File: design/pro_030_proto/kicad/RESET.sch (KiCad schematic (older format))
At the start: 13 parts, among them IC13 555N, IC8 74LS01N

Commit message: Add IO and XVID glue etc.
* Add IO Select glue
* Add Xosera glue
* Add new glues to schematic
* Clean up libs
* Reannotate (again)
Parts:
- renumbered C18 to C20, C19 to C21, IC8 to IC14, IC13 to IC15
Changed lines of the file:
@@
 AR Path="/5E53B952/6104F00C" Ref="IC?"  Part="1"
 AR Path="/60FBFA5C/6104F00C" Ref="IC?"  Part="1"
-AR Path="/61043B8D/6104F00C" Ref="IC13"  Part="1"
-F 0 "IC13" H 3850 4130 59  0000 L BNN
+AR Path="/61043B8D/6104F00C" Ref="IC15"  Part="1"
+F 0 "IC15" H 3850 4130 59  0000 L BNN
 F 1 "555N" H 3850 3195 59  0000 L BNN
 F 2 "Package_DIP:DIP-8_W7.62mm_LongPads" H 4150 3700 50  0001 C CNN
@@
 AR Path="/5E53B952/6104F012" Ref="IC?"  Part="1"
 AR Path="/60FBFA5C/6104F012" Ref="IC?"  Part="1"
-AR Path="/61043B8D/6104F012" Ref="IC8"  Part="1"
-F 0 "IC8" H 5900 4925 59  0000 L BNN
+AR Path="/61043B8D/6104F012" Ref="IC14"  Part="1"
+F 0 "IC14" H 5900 4925 59  0000 L BNN
 F 1 "74LS01N" H 5900 4600 59  0001 L BNN
 F 2 "Package_DIP:DIP-14_W7.62mm_Socket_LongPads" H 5800 4800 50  0001 C CNN
@@
 AR Path="/5E53B952/6104F018" Ref="IC?"  Part="2"
 AR Path="/60FBFA5C/6104F018" Ref="IC?"  Part="2"
-AR Path="/61043B8D/6104F018" Ref="IC8"  Part="2"
-F 0 "IC8" H 5900 5425 59  0000 L BNN
+AR Path="/61043B8D/6104F018" Ref="IC14"  Part="2"
+F 0 "IC14" H 5900 5425 59  0000 L BNN
 F 1 "74LS01N" H 5900 5100 59  0001 L BNN
 F 2 "Package_DIP:DIP-14_W7.62mm_Socket_LongPads" H 5800 5300 50  0001 C CNN
@@
 AR Path="/5E53B952/6104F01E" Ref="IC?"  Part="3"
 AR Path="/60FBFA5C/6104F01E" Ref="IC?"  Part="3"
-AR Path="/61043B8D/6104F01E" Ref="IC8"  Part="3"
-F 0 "IC8" H 6700 3825 59  0000 L BNN
+AR Path="/61043B8D/6104F01E" Ref="IC14"  Part="3"
+F 0 "IC14" H 6700 3825 59  0000 L BNN
 F 1 "74LS01N" H 6700 3500 59  0001 L BNN
 F 2 "Package_DIP:DIP-14_W7.62mm_Socket_LongPads" H 6600 3700 50  0001 C CNN
@@
 AR Path="/5E53B952/6104F048" Ref="C?"  Part="1"
 AR Path="/60FBFA5C/6104F048" Ref="C?"  Part="1"
-AR Path="/61043B8D/6104F048" Ref="C19"  Part="1"
-F 0 "C19" H 3210 2715 59  0000 L BNN
+AR Path="/61043B8D/6104F048" Ref="C21"  Part="1"
+F 0 "C21" H 3210 2715 59  0000 L BNN
 F 1 "100nF" H 3210 2515 59  0000 L BNN
 F 2 "Capacitor_THT:C_Rect_L4.0mm_W2.5mm_P2.50mm" H 3150 2700 50  0001 C CNN
@@
 AR Path="/5E53B952/6104F06C" Ref="C?"  Part="1"
 AR Path="/60FBFA5C/6104F06C" Ref="C?"  Part="1"
-AR Path="/61043B8D/6104F06C" Ref="C18"  Part="1"
-F 0 "C18" H 2795 4119 59  0000 L BNN
+AR Path="/61043B8D/6104F06C" Ref="C20"  Part="1"
+F 0 "C20" H 2795 4119 59  0000 L BNN
 F 1 "100uF" H 2795 3919 59  0000 L BNN
 F 2 "rosco_m68k:C-Electolytic-2,5-5" H 2750 4100 50  0001 C CNN
@@
 NoConn ~ 4550 3600
 $Comp
-L power:GND #PWR036
+L power:GND #PWR038
 U 1 1 6104F076
 P 4850 5700
-F 0 "#PWR036" H 4850 5450 50  0001 C CNN
+F 0 "#PWR038" H 4850 5450 50  0001 C CNN
 F 1 "GND" H 4855 5527 50  0000 C CNN
 F 2 "" H 4850 5700 50  0001 C CNN
@@
 	4850 5200 4850 5700
 $Comp
-L power:VCC #PWR034
+L power:VCC #PWR036
 U 1 1 6104F07D
 P 3550 2200
-F 0 "#PWR034" H 3550 2050 50  0001 C CNN
+F 0 "#PWR036" H 3550 2050 50  0001 C CNN
 F 1 "VCC" H 3567 2373 50  0000 C CNN
 F 2 "" H 3550 2200 50  0001 C CNN
@@
 $EndComp
 $Comp
-L power:VCC #PWR035
+L power:VCC #PWR037
 U 1 1 6104F083
 P 4650 2200
-F 0 "#PWR035" H 4650 2050 50  0001 C CNN
+F 0 "#PWR037" H 4650 2050 50  0001 C CNN
 F 1 "VCC" H 4667 2373 50  0000 C CNN
 F 2 "" H 4650 2200 50  0001 C CNN
@@
 $EndComp
 $Comp
-L power:VCC #PWR037
+L power:VCC #PWR039
 U 1 1 6104F089
 P 8500 2200
-F 0 "#PWR037" H 8500 2050 50  0001 C CNN
+F 0 "#PWR039" H 8500 2050 50  0001 C CNN
 F 1 "VCC" H 8517 2373 50  0000 C CNN
 F 2 "" H 8500 2200 50  0001 C CNN
@@
 	3550 2200 3550 3600
 $Comp
-L power:VCC #PWR033
+L power:VCC #PWR035
 U 1 1 6104F0A4
 P 3150 2200
-F 0 "#PWR033" H 3150 2050 50  0001 C CNN
+F 0 "#PWR035" H 3150 2050 50  0001 C CNN
 F 1 "VCC" H 3167 2373 50  0000 C CNN
 F 2 "" H 3150 2200 50  0001 C CNN
@@
 $EndComp
 $Comp
-L power:VCC #PWR032
+L power:VCC #PWR034
 U 1 1 6104F0AA
 P 2750 2200
-F 0 "#PWR032" H 2750 2050 50  0001 C CNN
+F 0 "#PWR034" H 2750 2050 50  0001 C CNN
 F 1 "VCC" H 2767 2373 50  0000 C CNN
 F 2 "" H 2750 2200 50  0001 C CNN

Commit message: Lots of work
* Sort out power and reset circuits, add ATX
* Add PCF8584 and supporting GAL code
* Stub out ATX board outline in PCB
* Various other tidying up and prep for layout
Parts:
- added unit 5 of IC14
- added J23: RESET_SW, Connector_PinHeader_2.54mm:PinHeader_2x01_P2.54mm_Vertical, symbol Connector:Conn_01x02_Male
- IC14: value 74LS01N -> 74LS05; symbol rosco_m68k-eagle-import:7401N -> 74xx:74LS05
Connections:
- net HALT: now also IC14.2, IC14.5; no longer IC14.1 (O), IC14.8 (I0), IC14.9 (I1)
- net at C20.+, IC15.2 (TR), IC15.6 (THR)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: now also IC14.10, J23.2 (Pin_2)
- net at LED1.K (C): now also IC14.6; no longer IC14.10 (O)
- net at R28.2, S1.3 (P): now also J23.1 (Pin_1)
- new net: IC14.1, IC14.3, IC15.3 (Q)
- new net PWR_GD: IC14.11
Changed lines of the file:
@@
 $Descr A4 11693 8268
 encoding utf-8
-Sheet 8 13
+Sheet 8 15
 Title "rosco_m68k Pro (030) Prototype"
-Date "2021-07-24"
+Date "2021-10-01"
 Rev "0"
 Comp "The Really Old-School Company Limited"
@@
 Wire Wire Line
 	6100 4800 6200 4800
-Wire Wire Line
-	6300 3800 6200 3800
-Wire Wire Line
-	6200 3800 6200 3600
-Wire Wire Line
-	6200 3600 6300 3600
-Connection ~ 6200 3800
 Text GLabel 9650 4800 2    67   Output ~ 0
 HALT
@@
 	7450 3200 7450 3000
 Wire Wire Line
-	5200 4800 5400 4800
-Wire Wire Line
-	5400 4800 5400 4700
-Wire Wire Line
-	5400 4700 5500 4700
-Wire Wire Line
-	5400 4800 5400 4900
-Wire Wire Line
-	5400 4900 5500 4900
-Wire Wire Line
 	5200 4800 5200 5300
-Wire Wire Line
-	5200 5300 5400 5300
-Wire Wire Line
-	5400 5300 5400 5200
-Wire Wire Line
-	5400 5200 5500 5200
-Wire Wire Line
-	5400 5300 5400 5400
-Wire Wire Line
-	5400 5400 5500 5400
-Connection ~ 5400 4800
-Connection ~ 5400 5300
 Connection ~ 5200 4800
 Wire Wire Line
-	4050 5200 4250 5200
+	4050 5200 4150 5200
 Wire Wire Line
 	4550 3800 4850 3800
@@
 	2350 4900 2350 3400
 Wire Wire Line
-	3650 5200 3050 5200
+	3650 5200 3350 5200
 Wire Wire Line
 	3050 5200 3050 4900
@@
 $EndComp
 $Comp
-L rosco_m68k-eagle-import:7401N IC?
+L 74xx:74LS05 IC?
 U 1 1 6104F012
 P 5800 4800
@@
 AR Path="/61043B8D/6104F012" Ref="IC14"  Part="1"
 F 0 "IC14" H 5900 4925 59  0000 L BNN
-F 1 "74LS01N" H 5900 4600 59  0001 L BNN
+F 1 "74LS05" H 5900 4600 59  0001 L BNN
 F 2 "Package_DIP:DIP-14_W7.62mm_Socket_LongPads" H 5800 4800 50  0001 C CNN
 F 3 "" H 5800 4800 50  0001 C CNN
@@
 $EndComp
 $Comp
-L rosco_m68k-eagle-import:7401N IC?
+L 74xx:74LS05 IC?
 U 2 1 6104F018
 P 5800 5300
@@
 AR Path="/61043B8D/6104F018" Ref="IC14"  Part="2"
 F 0 "IC14" H 5900 5425 59  0000 L BNN
-F 1 "74LS01N" H 5900 5100 59  0001 L BNN
+F 1 "74LS05" H 5900 5100 59  0001 L BNN
 F 2 "Package_DIP:DIP-14_W7.62mm_Socket_LongPads" H 5800 5300 50  0001 C CNN
 F 3 "" H 5800 5300 50  0001 C CNN
@@
 $EndComp
 $Comp
-L rosco_m68k-eagle-import:7401N IC?
+L 74xx:74LS05 IC?
 U 3 1 6104F01E
 P 6600 3700
@@
 AR Path="/61043B8D/6104F01E" Ref="IC14"  Part="3"
 F 0 "IC14" H 6700 3825 59  0000 L BNN
-F 1 "74LS01N" H 6700 3500 59  0001 L BNN
+F 1 "74LS05" H 6700 3500 59  0001 L BNN
 F 2 "Package_DIP:DIP-14_W7.62mm_Socket_LongPads" H 6600 3700 50  0001 C CNN
 F 3 "" H 6600 3700 50  0001 C CNN
@@
 	4650 2200 4650 4000
 Wire Wire Line
-	6200 3800 6200 4800
-Wire Wire Line
 	9150 3000 9150 5300
 Wire Wire Line
@@
 Wire Wire Line
 	8050 5300 9150 5300
+$Comp
+L 74xx:74LS05 IC?
+U 5 1 615FC564
+P 1900 4900
+AR Path="/615FC564" Ref="IC?"  Part="3"
+AR Path="/5E53B952/615FC564" Ref="IC?"  Part="3"
+AR Path="/60FBFA5C/615FC564" Ref="IC?"  Part="3"
+AR Path="/61043B8D/615FC564" Ref="IC14"  Part="5"
+F 0 "IC14" H 2000 5025 59  0000 L BNN
+F 1 "74LS05" H 2000 4700 59  0001 L BNN
+F 2 "Package_DIP:DIP-14_W7.62mm_Socket_LongPads" H 1900 4900 50  0001 C CNN
+F 3 "" H 1900 4900 50  0001 C CNN
+	5    1900 4900
+	1    0    0    -1
+$EndComp
+Text GLabel 1300 4900 0    50   Input ~ 0
+PWR_GD
+Wire Wire Line
+	2200 4900 2350 4900
+Connection ~ 2350 4900
+Wire Wire Line
+	1300 4900 1600 4900
+Wire Wire Line
+	5200 5300 5500 5300
+Wire Wire Line
+	5200 4800 5500 4800
+Wire Wire Line
+	6200 3700 6300 3700
+Wire Wire Line
+	6200 3700 6200 4800
+Connection ~ 3350 5200
+Wire Wire Line
+	3350 5200 3050 5200
+$Comp
+L Connector:Conn_01x02_Male J23
+U 1 1 6172EF3B
+P 3900 5600
+F 0 "J23" V 4200 5500 50  0000 L CNN
+F 1 "RESET_SW" V 4300 5350 50  0000 L CNN
+F 2 "Connector_PinHeader_2.54mm:PinHeader_2x01_P2.54mm_Vertical" H 3900 5600 50  0001 C CNN
+F 3 "~" H 3900 5600 50  0001 C CNN
+	1    3900 5600
+	0    1    1    0
+$EndComp
+Wire Wire Line
+	3800 5800 3350 5800
+Wire Wire Line
+	3350 5200 3350 5800
+Wire Wire Line
+	3900 5800 4150 5800
+Wire Wire Line
+	4150 5800 4150 5200
+Connection ~ 4150 5200
+Wire Wire Line
+	4150 5200 4250 5200
 $EndSCHEMATC

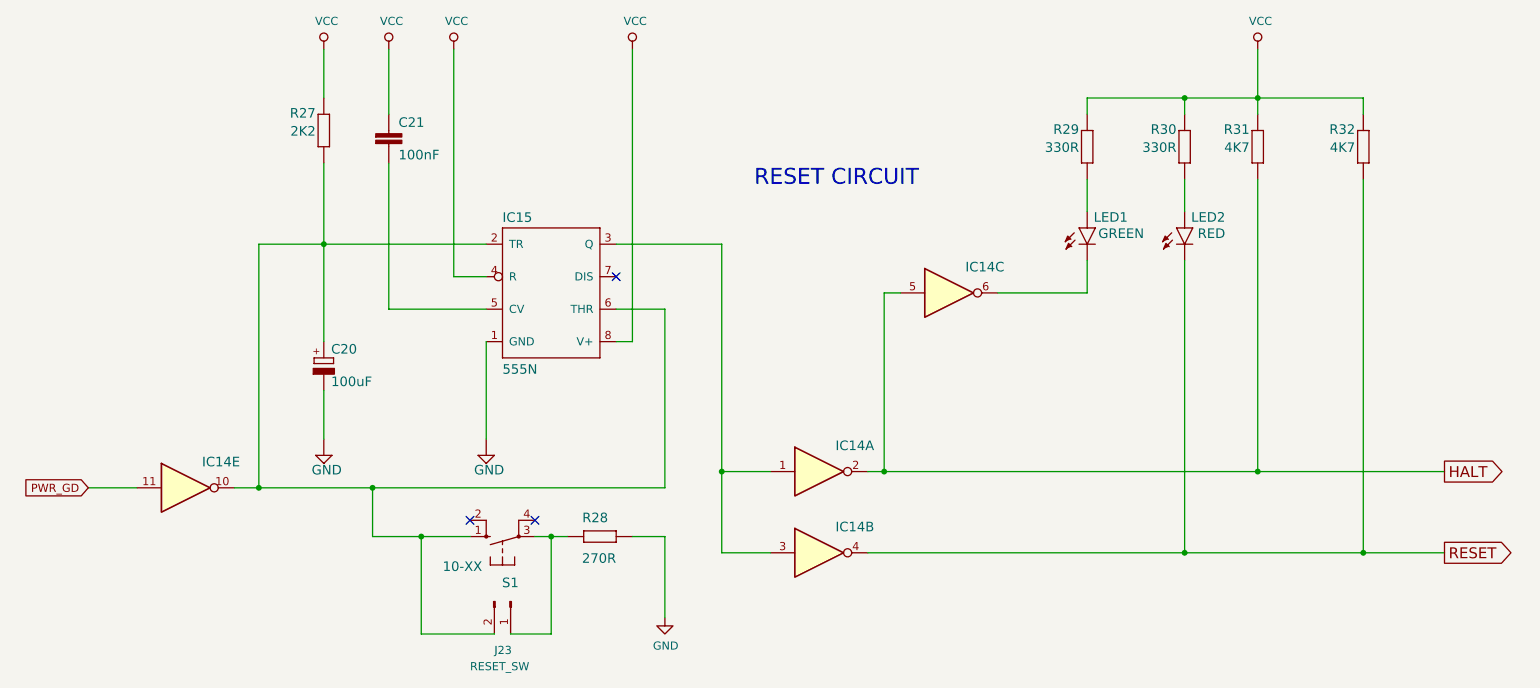
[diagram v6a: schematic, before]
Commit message: Add IC14 GAL into schematic
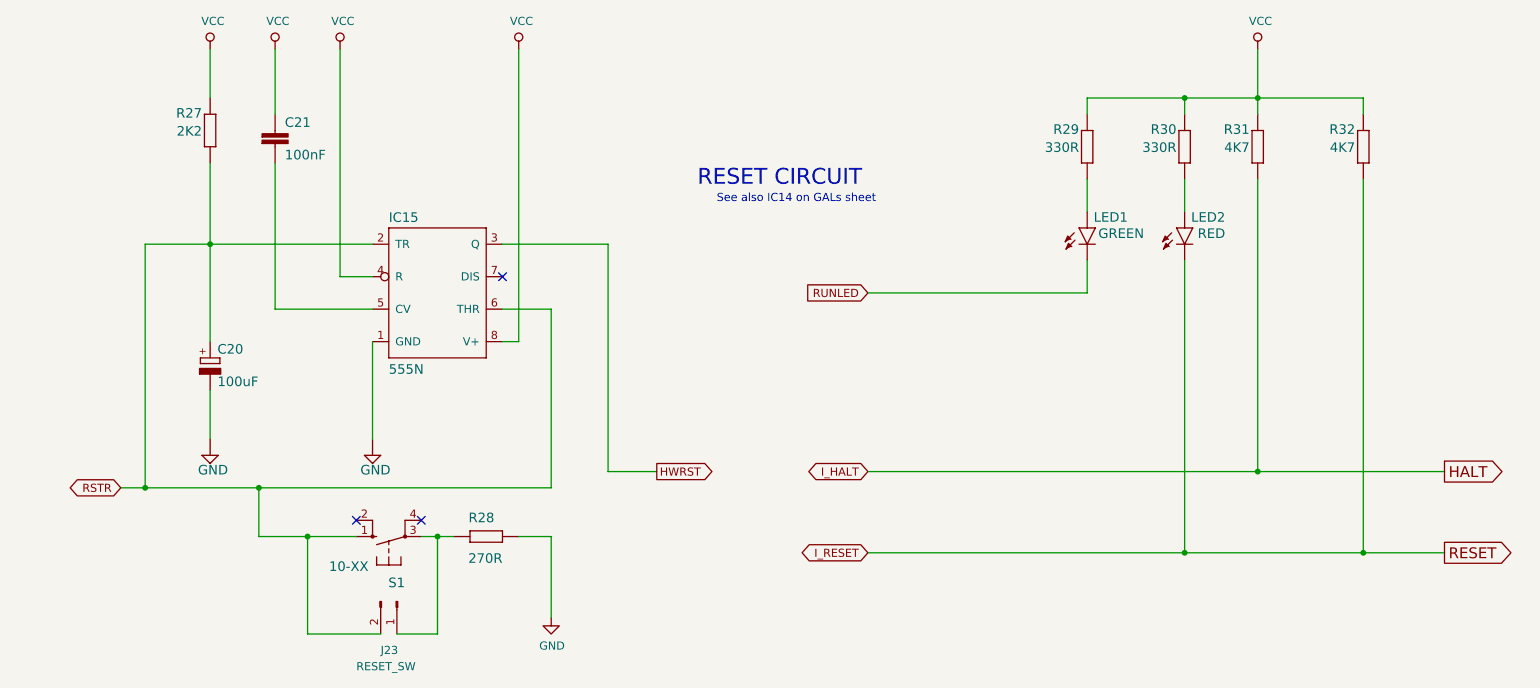
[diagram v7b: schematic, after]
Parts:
- removed IC14: 74LS05, Package_DIP:DIP-14_W7.62mm_Socket_LongPads, symbol 74xx:74LS05
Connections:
- net RSTR: now reaches C20.+, IC15.2 (TR), IC15.6 (THR), J23.2 (Pin_2), R27.1, S1.1 (S)
- net HWRST: now reaches IC15.3 (Q)
- net RUNLED: now reaches LED1.K (C)
- net RESET renamed I_RESET
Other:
- note added: "See also IC14 on GALs sheet"
- moved on the sheet: C20, C21, IC15, J23, R27, R28, S1

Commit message: Fix some silly mistakes
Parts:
- R31, R32: value 4K7 -> 1K2
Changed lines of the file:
@@
 AR Path="/61043B8D/6104F036" Ref="R31"  Part="1"
 F 0 "R31" V 8641 2850 59  0000 L BNN
-F 1 "4K7" V 8530 2850 59  0000 L BNN
+F 1 "1K2" V 8530 2850 59  0000 L BNN
 F 2 "rosco_m68k:R-0207_10" H 8500 2800 50  0001 C CNN
 F 3 "" H 8500 2800 50  0001 C CNN
@@
 AR Path="/61043B8D/6104F03C" Ref="R32"  Part="1"
 F 0 "R32" V 9291 2850 59  0000 L BNN
-F 1 "4K7" V 9180 2850 59  0000 L BNN
+F 1 "1K2" V 9180 2850 59  0000 L BNN
 F 2 "rosco_m68k:R-0207_10" H 9150 2800 50  0001 C CNN
 F 3 "" H 9150 2800 50  0001 C CNN
